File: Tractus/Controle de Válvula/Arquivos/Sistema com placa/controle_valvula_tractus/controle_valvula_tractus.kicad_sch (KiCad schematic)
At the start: 38 parts, among them J1 Conn_02x04_Top_Bottom, J2 Conn_02x02_Top_Bottom, U1 R7FA4M1AB3CFM_AA0

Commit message: Alteração de arquivos do esquemático e pcb
Alteração de arquivos do esquemático e pcb
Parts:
- renumbered C9 to C10, C10 to C11, C11 to C6, C6 to C7, C7 to C8, C8 to C9, J1 to DISPLAY1, J2 to FONTE|VALVULA1, R7 to R10, R8 to R11, R9 to R12, R10 to R13, R11 to R14, R12 to R15, R13 to R16, R16 to R2, R15 to R3, R2 to R4, R14 to R5, R3 to R6, R4 to R7, R5 to R8, R6 to R9

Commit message: Adding Files from e² studio
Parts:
- added C12: 1uF, Capacitor_SMD:C_1206_3216Metric, symbol Device:C
- added R17: 10K, Resistor_SMD:R_1206_3216Metric, symbol Device:R
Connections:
- net AMPOP_I: now also U1.51 (P502), R17.1; no longer AMP1.3 (+), U1.53 (P014)
- net GND: now also C12.1
- new net: AMP1.3 (+), C12.2, R17.2
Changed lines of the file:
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@@
 	)
 	(junction
+		(at 158.75 80.01)
+		(diameter 0)
+		(color 0 0 0 0)
+	)
+	(junction
 		(at 113.03 38.1)
 		(diameter 0)
@@
 	)
 	(junction
+		(at 170.18 72.39)
+		(diameter 0)
+		(color 0 0 0 0)
+	)
+	(junction
 		(at 22.86 45.72)
 		(diameter 0)
@@
 	(wire
 		(pts
-			(xy 163.83 72.39) (xy 175.26 72.39)
-		)
-		(stroke
-			(width 0)
-			(type default)
-		)
-	)
-	(wire
-		(pts
 			(xy 208.28 140.97) (xy 209.55 140.97)
 		)
@@
 	(wire
 		(pts
+			(xy 160.02 72.39) (xy 158.75 72.39)
+		)
+		(stroke
+			(width 0)
+			(type default)
+		)
+	)
+	(wire
+		(pts
 			(xy 92.71 38.1) (xy 113.03 38.1)
 		)
@@
 		)
 	)
+	(wire
+		(pts
+			(xy 158.75 72.39) (xy 158.75 80.01)
+		)
+		(stroke
+			(width 0)
+			(type default)
+		)
+	)
 	(polyline
 		(pts
@@
 		)
 	)
+	(wire
+		(pts
+			(xy 170.18 72.39) (xy 175.26 72.39)
+		)
+		(stroke
+			(width 0)
+			(type default)
+		)
+	)
 	(polyline
 		(pts
@@
 	(wire
 		(pts
+			(xy 167.64 72.39) (xy 170.18 72.39)
+		)
+		(stroke
+			(width 0)
+			(type default)
+		)
+	)
+	(wire
+		(pts
 			(xy 100.33 48.26) (xy 109.22 48.26)
 		)
@@
 	(wire
 		(pts
-			(xy 161.29 69.85) (xy 163.83 69.85)
+			(xy 158.75 55.88) (xy 162.56 55.88)
 		)
 		(stroke
@@
 	(wire
 		(pts
-			(xy 189.23 39.37) (xy 201.93 39.37)
+			(xy 170.18 62.23) (xy 170.18 72.39)
 		)
 		(stroke
@@
 	(wire
 		(pts
-			(xy 163.83 69.85) (xy 163.83 72.39)
+			(xy 189.23 39.37) (xy 201.93 39.37)
 		)
 		(stroke
@@
 	(wire
 		(pts
-			(xy 194.31 118.11) (xy 201.93 118.11)
+			(xy 162.56 55.88) (xy 162.56 62.23)
 		)
 		(stroke
@@
 	(wire
 		(pts
-			(xy 175.26 39.37) (xy 189.23 39.37)
+			(xy 194.31 118.11) (xy 201.93 118.11)
 		)
 		(stroke
@@
 	(wire
 		(pts
-			(xy 22.86 45.72) (xy 27.94 45.72)
+			(xy 175.26 39.37) (xy 189.23 39.37)
 		)
 		(stroke
@@
 	(wire
 		(pts
-			(xy 102.87 35.56) (xy 100.33 35.56)
+			(xy 22.86 45.72) (xy 27.94 45.72)
 		)
 		(stroke
@@
 	(wire
 		(pts
-			(xy 208.28 148.59) (xy 208.28 147.32)
+			(xy 102.87 35.56) (xy 100.33 35.56)
 		)
 		(stroke
@@
 	(wire
 		(pts
-			(xy 201.93 39.37) (xy 213.36 39.37)
+			(xy 208.28 148.59) (xy 208.28 147.32)
 		)
 		(stroke
@@
 	(wire
 		(pts
-			(xy 173.99 135.89) (xy 173.99 137.16)
+			(xy 201.93 39.37) (xy 213.36 39.37)
 		)
 		(stroke
@@
 	(wire
 		(pts
-			(xy 25.4 73.66) (xy 41.91 73.66)
+			(xy 173.99 135.89) (xy 173.99 137.16)
 		)
 		(stroke
@@
 		)
 	)
-	(label "AMPOP_I"
-		(at 25.4 73.66 0)
-		(effects
-			(font
-				(size 1.27 1.27)
-			)
-			(justify left bottom)
-		)
-	)
 	(label "SPI_SCK"
 		(at 41.91 83.82 180)
@@
 	)
 	(label "AMPOP_I"
-		(at 161.29 69.85 0)
+		(at 158.75 55.88 0)
 		(effects
 			(font
@@
 		)
 	)
+	(label "AMPOP_I"
+		(at 92.71 114.3 0)
+		(effects
+			(font
+				(size 1.27 1.27)
+			)
+			(justify left bottom)
+		)
+	)
 	(label "SPI_MOSI"
 		(at 194.31 120.65 0)
@@
 	)
 	(symbol
+		(lib_id "Device:R")
+		(at 166.37 62.23 90)
+		(unit 1)
+		(body_style 1)
+		(exclude_from_sim no)
+		(in_bom yes)
+		(on_board yes)
+		(in_pos_files yes)
+		(dnp no)
+		(property "Reference" "R17"
+			(at 166.37 62.23 90)
+			(show_name no)
+			(do_not_autoplace no)
+			(effects
+				(font
+					(size 1.27 1.27)
+				)
+			)
+		)
+		(property "Value" "10K"
+			(at 166.37 59.944 90)
+			(show_name no)
+			(do_not_autoplace no)
+			(effects
+				(font
+					(size 1.27 1.27)
+				)
+			)
+		)
+		(property "Footprint" "Resistor_SMD:R_1206_3216Metric"
+			(at 166.37 64.008 90)
+			(hide yes)
+			(show_name no)
+			(do_not_autoplace no)
+			(effects
+				(font
+					(size 1.27 1.27)
+				)
+			)
+		)
+		(property "Datasheet" ""
+			(at 166.37 62.23 0)
+			(hide yes)
+			(show_name no)
+			(do_not_autoplace no)
+			(effects
+				(font
+					(size 1.27 1.27)
+				)
+			)
+		)
+		(property "Description" "Resistor"
+			(at 166.37 62.23 0)
+			(hide yes)
+			(show_name no)
+			(do_not_autoplace no)
+			(effects
+				(font
+					(size 1.27 1.27)
+				)
+			)
+		)
+		(pin "1"
+		)
+		(pin "2"
+		)
+		(instances
+			(project "controle_valvula_tractus"
+				(path "/94d8a090-3841-4036-9d70-e62beca957c5"
+					(reference "R17")
+					(unit 1)
+				)
+			)
+		)
+	)
+	(symbol
 		(lib_id "Connector_Generic:Conn_02x02_Top_Bottom")
 		(at 257.81 73.66 0)
@@
 					(unit 1)
 				)
+			)
+		)
+	)
+	(symbol
+		(lib_id "Device:C")
+		(at 163.83 72.39 90)
+		(unit 1)
+		(body_style 1)
+		(exclude_from_sim no)
+		(in_bom yes)
+		(on_board yes)
+		(in_pos_files yes)
+		(dnp no)
+		(property "Reference" "C12"
+			(at 163.83 69.342 90)
+			(show_name no)
+			(do_not_autoplace no)
+			(effects
+				(font
+					(size 1.27 1.27)
+				)
+			)
+		)
+		(property "Value" "1uF"
+			(at 163.83 75.692 90)
+			(show_name no)
+			(do_not_autoplace no)
+			(effects
+				(font
+					(size 1.27 1.27)
+				)
+			)
+		)
+		(property "Footprint" "Capacitor_SMD:C_1206_3216Metric"
+			(at 167.64 71.4248 0)
+			(hide yes)
+			(show_name no)
+			(do_not_autoplace no)
+			(effects
+				(font
+					(size 1.27 1.27)
+				)
+			)
+		)
+		(property "Datasheet" ""
+			(at 163.83 72.39 0)
+			(hide yes)
+			(show_name no)
+			(do_not_autoplace no)
+			(effects
+				(font
+					(size 1.27 1.27)
+				)
+			)
+		)
+		(property "Description" "Unpolarized capacitor"
+			(at 163.83 72.39 0)
+			(hide yes)
+			(show_name no)
+			(do_not_autoplace no)
+			(effects
+				(font
+					(size 1.27 1.27)
+				)
+			)
+		)
+		(pin "2"
+		)
+		(pin "1"
+		)
+		(instances
+			(project "controle_valvula_tractus"
+				(path "/94d8a090-3841-4036-9d70-e62beca957c5"
+					(reference "C12")
+					(unit 1)
+				)

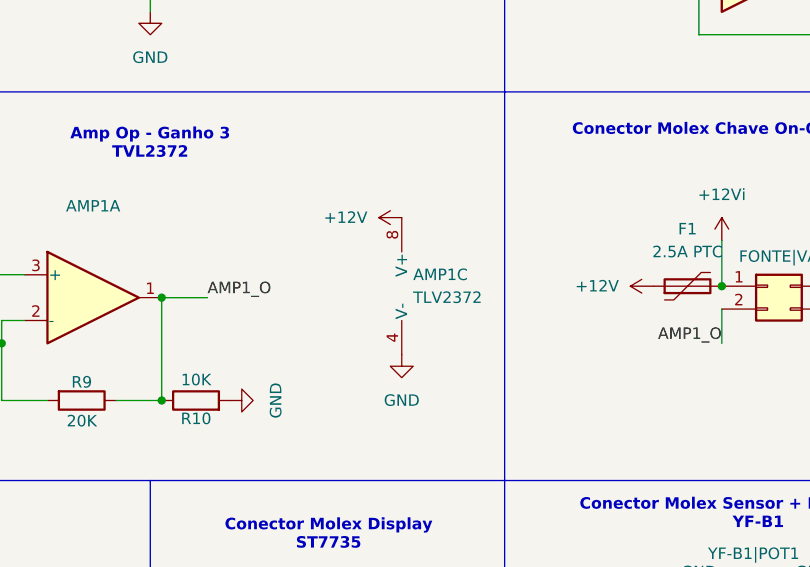
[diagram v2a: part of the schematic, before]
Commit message: Add op-amp decoupling and Uno PWM test
Updates the KiCad design to add C13 (100nF) and C14 (10uF) decoupling on the +12V rail near the op-amp section, with related schematic wiring, PCB routing, and reference updates. In the PlatformIO project, switches target from Uno R4 Minima to classic Uno, marks pioarduino as unwanted in VS Code recommendations, and replaces the previous LCD/flow-control sketch with a simple potentiometer-to-PWM output test program with serial monitoring.
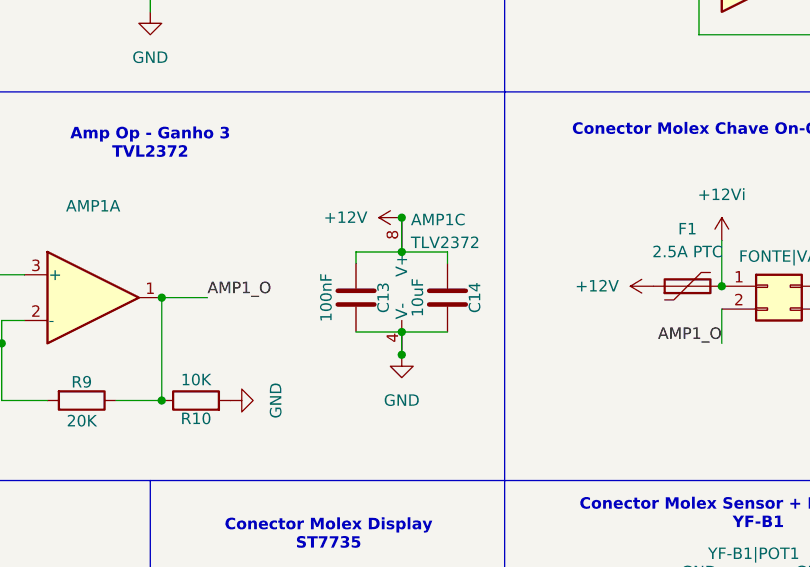
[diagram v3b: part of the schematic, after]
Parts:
- added C13: 100nF, Capacitor_SMD:C_1206_3216Metric, symbol Device:C
- added C14: 10uF, Capacitor_SMD:C_1206_3216Metric, symbol Device:C
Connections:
- net +12V: now also C13.1, C14.1
- net GND: now also C13.2, C14.2

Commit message: Atualizado diagrama da pcb
Mudanças para tornar o design mais organizado e limpo
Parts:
- C1, C3, C5, C6, C7: footprint Capacitor_SMD:C_0805_2012Metric -> Capacitor_SMD:C_0603_1608Metric
- C10: footprint Capacitor_SMD:C_1206_3216Metric -> Capacitor_SMD:C_0805_2012Metric
- C12, C13, C2, C4: footprint Capacitor_SMD:C_1206_3216Metric -> Capacitor_SMD:C_0603_1608Metric
- C8: renamed from C9; footprint Capacitor_SMD:C_1206_3216Metric -> Capacitor_SMD:C_0805_2012Metric
- C9: renamed from C8; footprint Capacitor_SMD:C_0805_2012Metric -> Capacitor_SMD:C_0603_1608Metric
- R1, R10, R11, R12, R13, R14, R15, R16, R17, R2, R3, R4, R5, R6, R7, R8, R9: footprint Resistor_SMD:R_1206_3216Metric -> Resistor_SMD:R_0603_1608Metric
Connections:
- net +12V: now also YF-B1|POT1.2 (Pin_2); no longer YF-B1|POT1.3 (Pin_3)
- net BLUE: now also U1.14 (P409); no longer U1.13 (P410)
- net GND: now also RGB1.1 (Pin_1), YF-B1|POT1.6 (Pin_6); no longer RGB1.4 (Pin_4), YF-B1|POT1.1 (Pin_1)
- net GREEN: now also U1.13 (P410); no longer U1.14 (P409)
- net POT_O: now also YF-B1|POT1.3 (Pin_3); no longer YF-B1|POT1.2 (Pin_2)
- net SENSOR_O: now also YF-B1|POT1.1 (Pin_1); no longer YF-B1|POT1.6 (Pin_6)
- net at R11.1: now also RGB1.4 (Pin_4); no longer RGB1.1 (Pin_1)
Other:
- moved on the sheet: R11

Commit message: Adicionado circuito de failsafe para fechamento da válvula
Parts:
- removed FONTE|VALVULA1: Conn_02x02_Top_Bottom, Connector_Molex:Molex_Mini-Fit_Jr_5566-04A_2x02_P4.20mm_Vertical, symbol Connector_Generic:Conn_02x02_Top_Bottom
- added C15, C16, C17, C18: 4.7F, Capacitor_THT:C_Radial_D12.5mm_H20.0mm_P5.00mm, symbol Device:C
- added D1, D2: D_Schottky, Diode_SMD:D_SMC, symbol Device:D_Schottky
- added D3: D_Zener, Diode_SMD:D_SMA, symbol Device:D_Zener
- added J1: FONTE|VALVE, Connector_Molex:Molex_Mini-Fit_Jr_5566-06A_2x03_P4.20mm_Vertical, symbol Connector_Generic:Conn_02x03_Top_Bottom
- added R18, R19, R24, R25: 20, Resistor_SMD:R_2512_6332Metric, symbol Device:R
- added R20, R21, R22, R23: 10K, Resistor_SMD:R_0603_1608Metric, symbol Device:R
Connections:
- net +12V: now also D1.2 (A)
- net +12Vi: now also J1.1 (Pin_1)
- net AMP1_O: now also J1.2 (Pin_2)
- net GND: now also C18.2, D3.2 (A), J1.5 (Pin_5), J1.6 (Pin_6), R23.2
- net at RGB1.2 (Pin_2): now also R13.1; no longer R12.1
- net VALVE_FB: now reaches U1.1 (P400)
- net VALVE_FB: now also J1.3 (Pin_3)
- net at RGB1.3 (Pin_3): now also R12.1; no longer R13.1
- new net: C15.1, D2.2 (A), D3.1 (K), R19.2, R20.1, R25.2
- new net: C15.2, C16.1, R20.2, R21.1
- new net: R24.2, R25.1
- new net: R18.2, R19.1
- new net: C17.2, C18.1, R22.2, R23.1
- new net: C16.2, C17.1, R21.2, R22.1
- new net +12V - Valve: D1.1 (K), D2.1 (K), J1.4 (Pin_4), R18.1, R24.1
